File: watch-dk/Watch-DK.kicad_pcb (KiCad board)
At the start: 4 copper layers, 100 x 70 mm, 116 parts, among them IC101 nPM1300-QEXX, IC201 APDS-9306-065, IC202 RV-8263-C8, IC203 BMI270, IC204 LIS2MDLTR, IC205 BMP581, IC206 DRV2603RUNT, IC301 FAN5624UMPX, IC302 MX25U51245GZ4I00, IC303 USBLC6-2P6, IC304 NTS0104GU12, M301 NORA-B106, Q201 DMG1013UW-7, Q202 PMZ550UNEYL, Q203 PMZ550UNEYL, X101 Battery, X102 Battery, X103 Power, X201 Power, X202 I2S, X203 Power, X204 I2C, X205 Power, X206 Power, X207 Power, X208 Power, X209 Power, X210 Motor, X301 Power, X302 Power, X303 Device, X304 GPIO, X305 UART, X306 IO Power, X307 Display, X308 Touch Power, X309 LED Power, X310 DEBUG

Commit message: Task: Issue #124
Signed-off-by: Daniel Kampert <DanielKampert@kampis-elektroecke.de>
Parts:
- TP103: value 1V8 -> +1V8
- TP104: value 3V0 -> +3V0
- moved C203 2.10 mm to (166.0, 130.3)
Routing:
- net +1V8: track 8.52 -> 6.32 mm
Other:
- board text added: "x"
- board text added: "y"
- board text removed: "1V8"
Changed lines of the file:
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@@
 			)
 		)
-		(property "Value" "1V8"
+		(property "Value" "+1V8"
 			(at 0 -1 90)
 			(layer "F.SilkS")
@@
 			)
 		)
-		(property "Value" "3V0"
+		(property "Value" "+3V0"
 			(at 0 -1 90)
 			(layer "F.SilkS")
@@
 			)
 		)
+		(property "manf" ""
+			(at 0 0 0)
+			(unlocked yes)
+			(layer "F.Fab")
+			(hide yes)
+			(effects
+				(font
+					(size 0.8 0.8)
+					(thickness 0.12)
+				)
+			)
+		)
+		(property "manf#" ""
+			(at 0 0 0)
+			(unlocked yes)
+			(layer "F.Fab")
+			(hide yes)
+			(effects
+				(font
+					(size 0.8 0.8)
+					(thickness 0.12)
+				)
+			)
+		)
+		(property "mouser#" ""
+			(at 0 0 0)
+			(unlocked yes)
+			(layer "F.Fab")
+			(hide yes)
+			(effects
+				(font
+					(size 0.8 0.8)
+					(thickness 0.12)
+				)
+			)
+		)
 		(property ki_fp_filters "Pin* Test*")
 		(sheetname "/Project Architecture/Power Management/")
@@
 	(footprint "Capacitor_SMD:C_0402_1005Metric"
 		(layer "F.Cu")
-		(at 164.1875 129.3 180)
+		(at 166.02 130.3325 180)
 		(descr "Capacitor SMD 0402 (1005 Metric), square (rectangular) end terminal, IPC-7351 nominal, (Body size source: IPC-SM-782 page 76, https://www.pcb-3d.com/wordpress/wp-content/uploads/ipc-sm-782a_amendment_1_and_2.pdf), generated with kicad-footprint-generator")
 		(tags "capacitor")
@@
 	)
 	(gr_line
+		(start 170.7 128.1365)
+		(end 170.573 128.3905)
+		(stroke
+			(width 0.15)
+			(type default)
+		)
+		(layer "F.SilkS")
+	)
+	(gr_line
 		(start 186.3 103.8)
 		(end 189.2 103.8)
@@
 	)
 	(gr_line
+		(start 170.7 128.1365)
+		(end 170.827 128.3905)
+		(stroke
+			(width 0.15)
+			(type default)
+		)
+		(layer "F.SilkS")
+	)
+	(gr_line
+		(start 170.7 128.1365)
+		(end 170.7 128.8)
+		(stroke
+			(width 0.15)
+			(type default)
+		)
+		(layer "F.SilkS")
+	)
+	(gr_line
 		(start 205.85 95.15)
 		(end 196.1 95.15)
@@
 	)
 	(gr_line
+		(start 170.065 128.8)
+		(end 170.319 128.673)
+		(stroke
+			(width 0.15)
+			(type default)
+		)
+		(layer "F.SilkS")
+	)
+	(gr_line
+		(start 170.065 128.8)
+		(end 170.7 128.8)
+		(stroke
+			(width 0.15)
+			(type default)
+		)
+		(layer "F.SilkS")
+	)
+	(gr_line
+		(start 170.065 128.8)
+		(end 170.319 128.927)
+		(stroke
+			(width 0.15)
+			(type default)
+		)
+		(layer "F.SilkS")
+	)
+	(gr_line
 		(start 189.2 103.85)
 		(end 189.2 111.65)
@@
 		)
 	)
-	(gr_text "1V8"
+	(gr_text "+1V8"
 		(at 141.1 127.38 0)
 		(layer "F.SilkS")
@@
 		)
 	)
+	(gr_text "y"
+		(at 169.7 128.6 0)
+		(layer "F.SilkS")
+		(effects
+			(font
+				(size 0.8 0.8)
+				(thickness 0.12)
+			)
+		)
+	)
 	(gr_text "+"
 		(at 191.3 94.6 0)
@@
 		)
 	)
-	(gr_text "1V8"
+	(gr_text "+1V8"
 		(at 131.6 124.98 0)
 		(layer "F.SilkS")
@@
 		)
 	)
+	(gr_text "x"
+		(at 170.7 127.6 0)
+		(layer "F.SilkS")
+		(effects
+			(font
+				(size 0.8 0.8)
+				(thickness 0.12)
+			)
+		)
+	)
 	(gr_text "Pressure"
 		(at 191 137.9 0)
@@
 	)
 	(segment
-		(start 163.7075 129.3)
-		(end 163 129.3)
+		(start 165.54 130.3325)
+		(end 164.8325 130.3325)
 		(width 0.2)
 		(layer "F.Cu")
@@
 	)
 	(via
-		(at 163 129.3)
+		(at 164.8325 130.3325)
 		(size 0.45)
 		(drill 0.25)
@@
 	)
 	(segment
-		(start 164.6675 129.8675)
-		(end 164.6675 129.3)
-		(width 0.2)
-		(layer "F.Cu")
-		(net 2)
-	)
-	(segment
 		(start 190.8 127.995)
 		(end 190.8 128.245)
@@
 	)
 	(segment
-		(start 166.6 129.9)
-		(end 166.4 130.1)
-		(width 0.2)
-		(layer "F.Cu")
-		(net 2)
-	)
-	(segment
 		(start 151.565 128.01)
 		(end 152.05 128.495)
@@
 	)
 	(segment
-		(start 164.9 130.1)
-		(end 164.6675 129.8675)
+		(start 166.5 130)
+		(end 166.5 130.3325)
 		(width 0.2)
 		(layer "F.Cu")
@@
 	)
 	(segment
-		(start 166.6 129.4625)
-		(end 166.6 129.9)
+		(start 186.6075 128.9875)
+		(end 186.62 128.975)
 		(width 0.2)
 		(layer "F.Cu")
@@
 	)
 	(segment
-		(start 186.6075 128.9875)
-		(end 186.62 128.975)
+		(start 151.2 128.01)
+		(end 151.565 128.01)
 		(width 0.2)
 		(layer "F.Cu")
@@
 	)
 	(segment
-		(start 151.2 128.01)
-		(end 151.565 128.01)
+		(start 166.6 129.4625)
+		(end 166.6 129.9)
 		(width 0.2)
 		(layer "F.Cu")
@@
 	)
 	(segment
-		(start 166.4 130.1)
-		(end 164.9 130.1)
+		(start 166.6 129.9)
+		(end 166.5 130)
 		(width 0.2)
 		(layer "F.Cu")
@@
 	)
 	(zone
-		(net 0)
-		(net_name "")
-		(layer "F.Cu")
-		(hatch edge 0.5)
-		(connect_pads
-			(clearance 0)
-		)
-		(min_thickness 0.25)
-		(filled_areas_thickness no)
-		(keepout
-			(tracks allowed)
-			(vias allowed)
-			(pads allowed)
-			(copperpour not_allowed)
-			(footprints allowed)
-		)
-		(placement
-			(enabled no)
-			(sheetname "")
-		)
-		(fill
-			(thermal_gap 0.5)
-			(thermal_bridge_width 0.5)
-		)
-		(polygon
-			(pts
-				(xy 164.4 129.5) (xy 164.4 130.1) (xy 164.7 130.4) (xy 166.6 130.4) (xy 166.9 130.1) (xy 166.9 129)
-				(xy 166.3 129) (xy 166.3 129.7) (xy 166.2 129.8) (xy 165.1 129.8) (xy 164.9 129.6) (xy 164.9 129.5)
-			)
-		)
-	)
-	(zone
 		(net 1)
 		(net_name "GND")
@@
 			)
 		)
+	)
+	(zone
+		(net 0)
+		(net_name "")
+		(layer "F.Cu")
+		(hatch edge 0.5)
+		(connect_pads
+			(clearance 0)
+		)
+		(min_thickness 0.25)
+		(filled_areas_thickness no)
+		(keepout
+			(tracks allowed)
+			(vias allowed)
+			(pads allowed)
+			(copperpour not_allowed)
+			(footprints allowed)
+		)
+		(placement
+			(enabled no)
+			(sheetname "")
+		)
+		(fill
+			(thermal_gap 0.5)
+			(thermal_bridge_width 0.5)
+		)
+		(polygon
+			(pts
+				(xy 166.9 129.1) (xy 166.9 130.3) (xy 166.32 130.3) (xy 166.32 129.1)
+			)
+		)

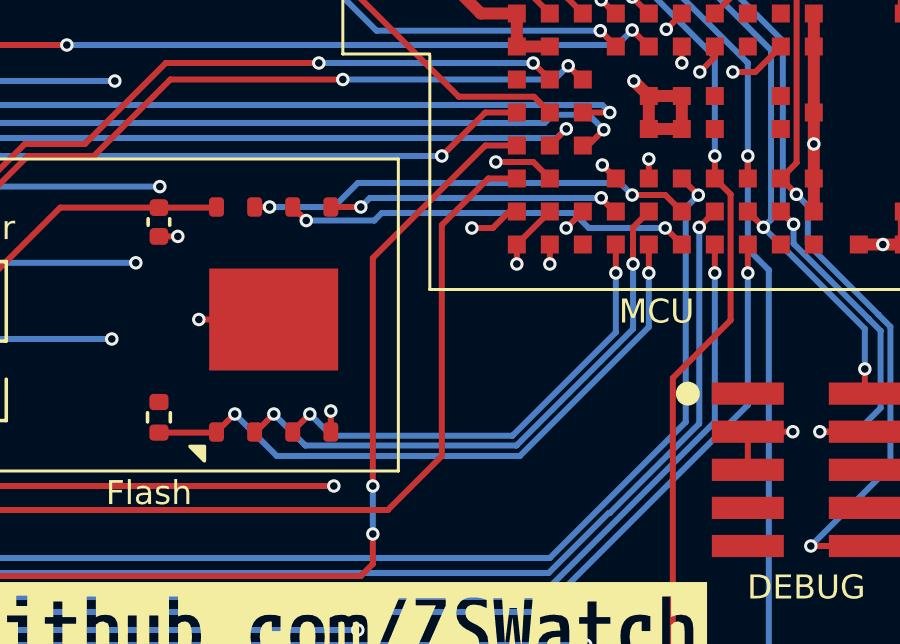
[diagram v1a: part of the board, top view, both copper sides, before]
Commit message: Increase length of QSPI Clock line to avoid timing issues
Signed-off-by: Daniel Kampert <DanielKampert@kampis-elektroecke.de>
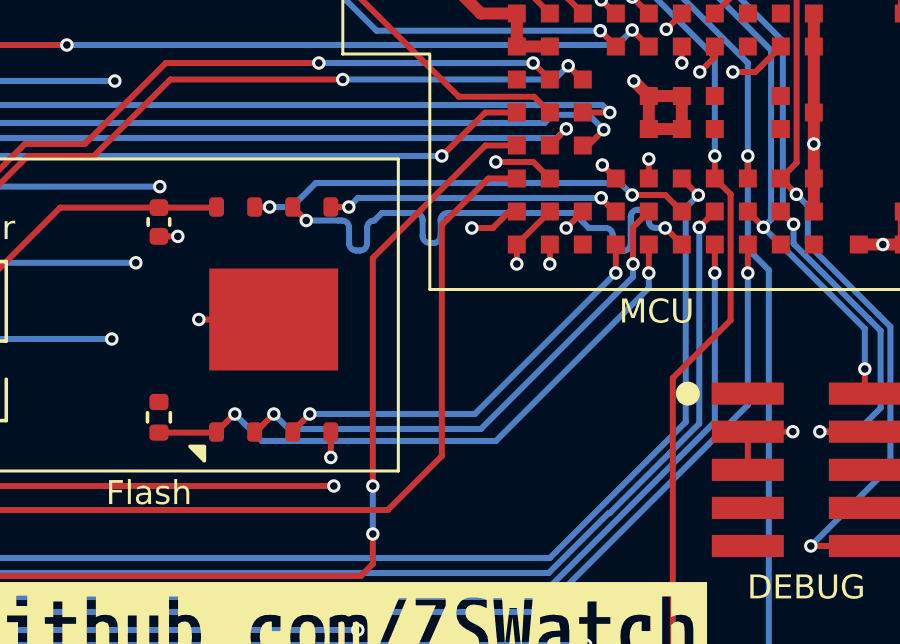
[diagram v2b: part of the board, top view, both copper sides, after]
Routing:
- net QSPI-CLK: track 13.7 -> 18.9 mm
- net QSPI-IO2: track 15.7 -> 13.9 mm
- net QSPI-IO1: track 19.0 -> 17.6 mm
- net QSPI-CS: track 21.7 -> 20.5 mm
